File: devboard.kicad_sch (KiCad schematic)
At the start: 28 parts, among them J1 USB4110-GF-A, J2 USB_BOOT, P1 TC2030-CTX, U1 RP2040, U2 NCP1117-3.3_SOT223, U3 AT25SF128A-SHB-T, Y1 ECS-2033-120-BN

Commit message: finished??
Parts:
- added H1, H10, H11, H12, H3, H4, H5, H6, H7, H8, H9: MountingHole_Pad, MountingHole:MountingHole_2.2mm_M2_Pad, symbol Mechanical:MountingHole_Pad
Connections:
- net GND: now also H1.1, H10.1, H11.1, H12.1, H3.1, H4.1, H5.1, H6.1, H7.1, H8.1, H9.1

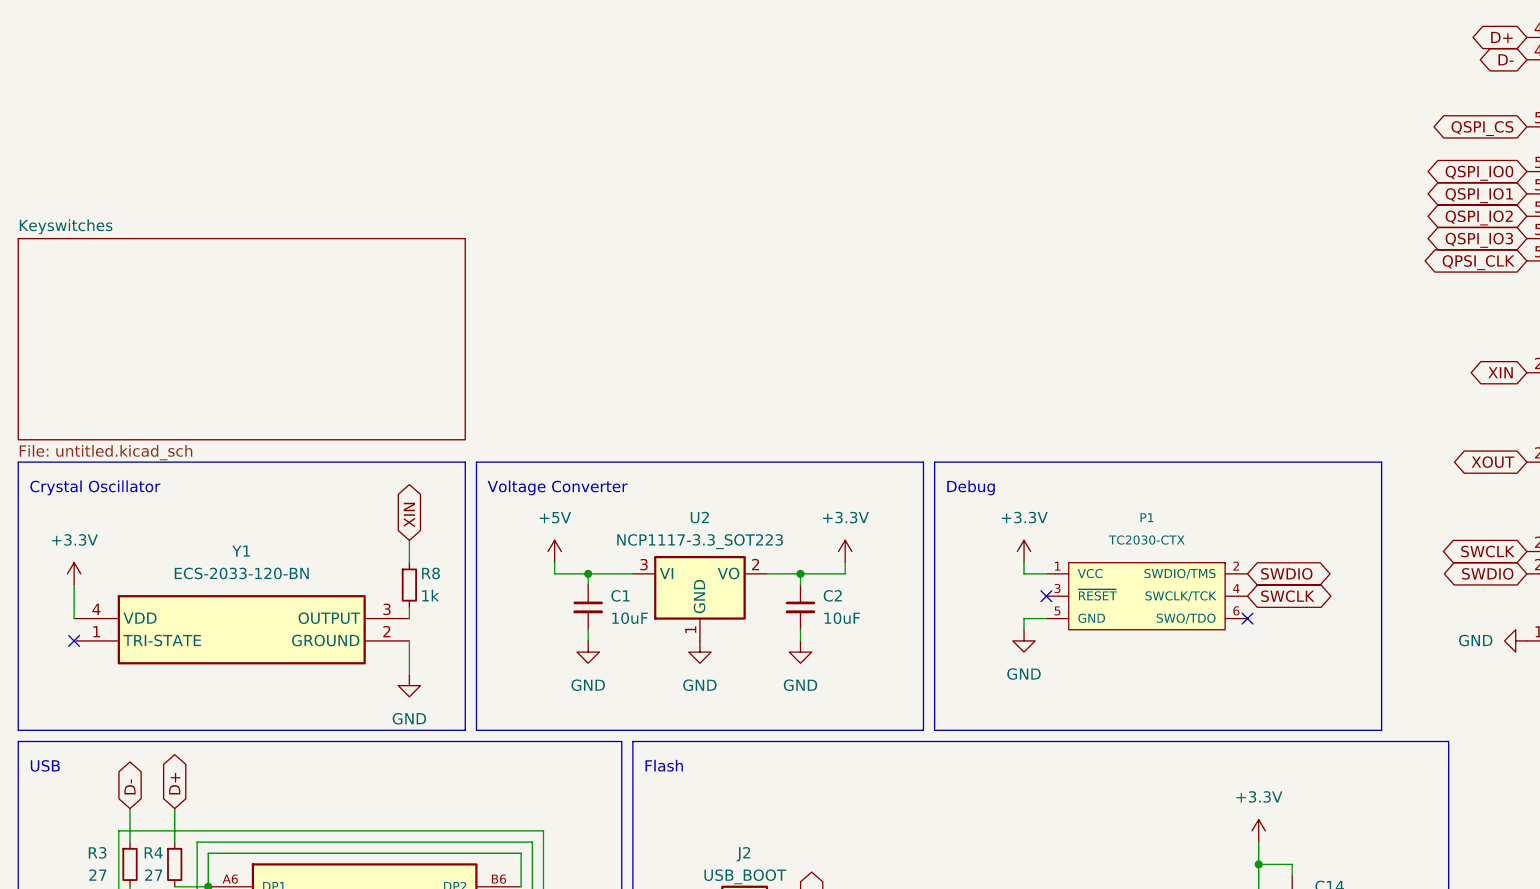
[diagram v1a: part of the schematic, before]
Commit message: Change LDO to DCDC Buck Converter
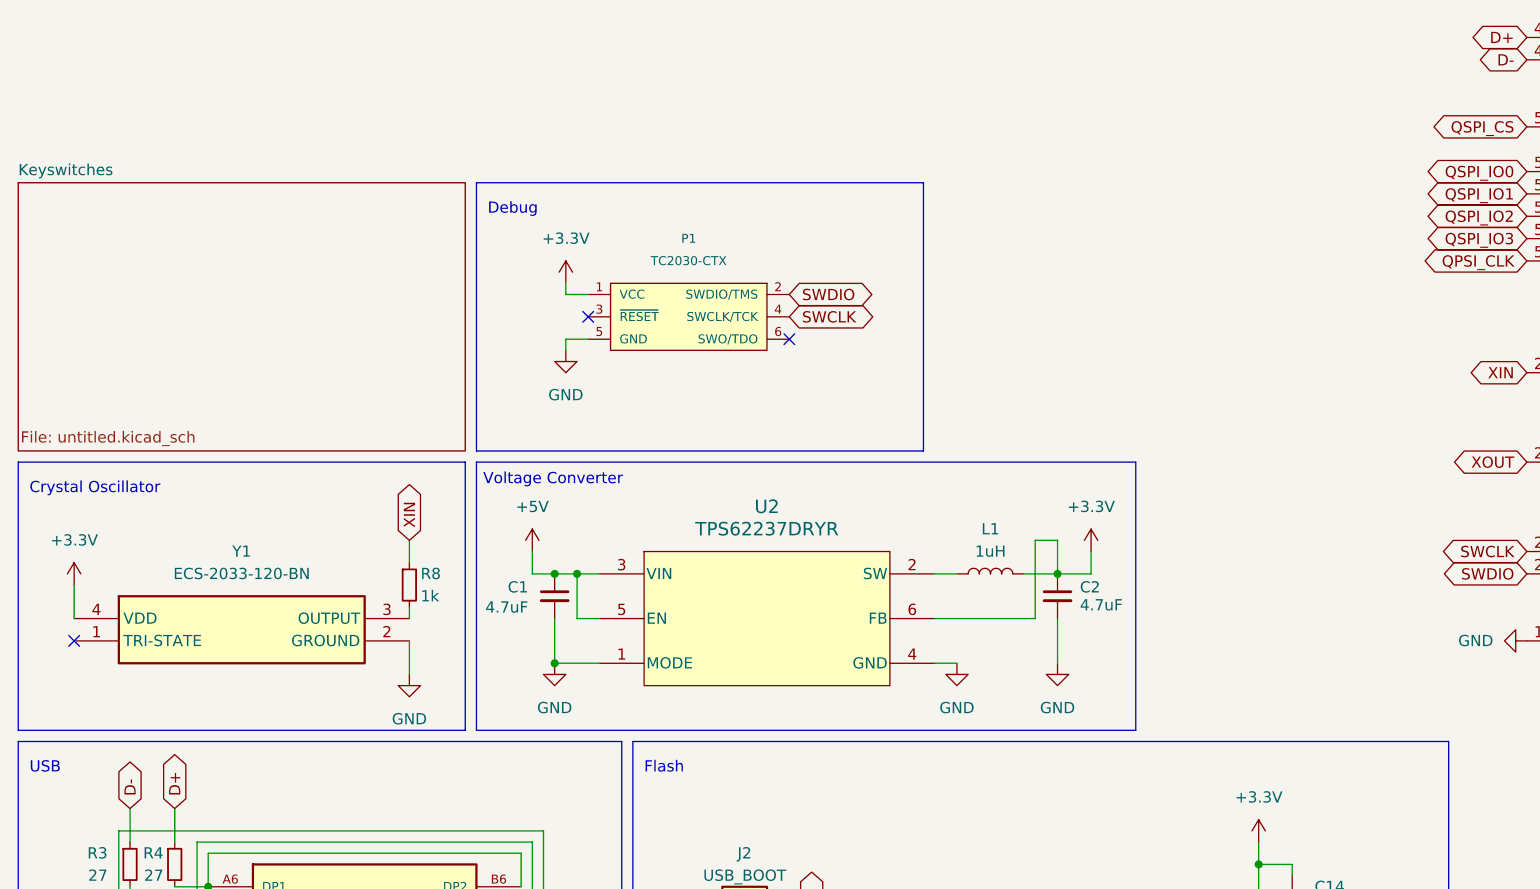
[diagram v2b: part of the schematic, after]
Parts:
- removed U2: NCP1117-3.3_SOT223, Package_TO_SOT_SMD:SOT-223-3_TabPin2, symbol Regulator_Linear:NCP1117-3.3_SOT223
- added L1: 1uH, Inductor_SMD:L_1008_2520Metric, symbol Device:L
- added U2: TPS62237DRYR, TPS62237:DRY0006A, symbol TPS62237:TPS62237DRYR
- C1, C2: value 10uF -> 4.7uF
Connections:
- net +3.3V: now also L1.2, U2.6 (FB)
- net +5V: now also U2.3 (VIN), U2.5 (EN)
- net GND: now also U2.1 (MODE), U2.4 (GND)
- new net: L1.1, U2.2 (SW)
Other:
- moved on the sheet: P1

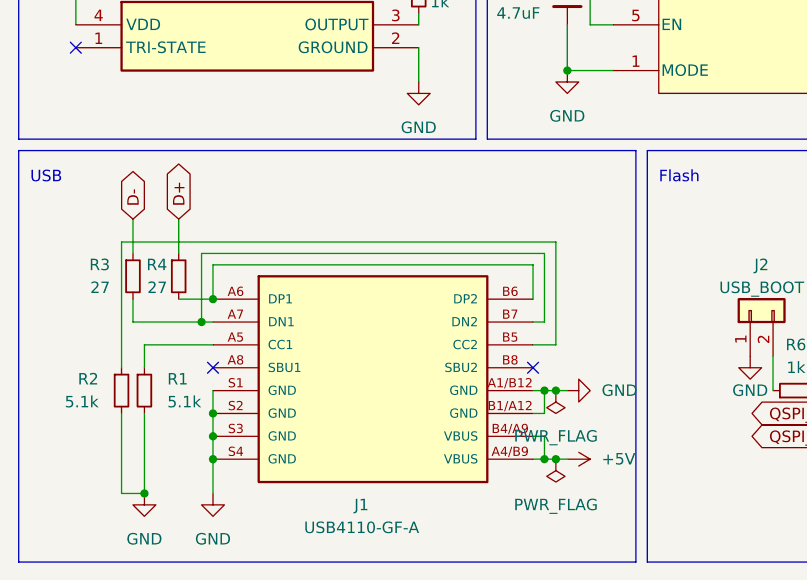
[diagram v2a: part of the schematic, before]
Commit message: Redo some routing and placement
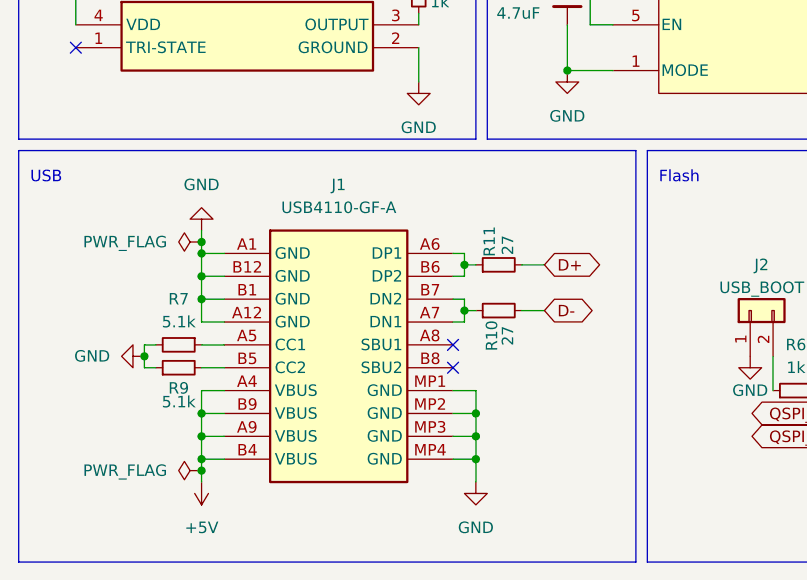
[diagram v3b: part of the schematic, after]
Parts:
- removed J1: USB4110-GF-A, 1A_Connectors:GCT_USB4110GFA, symbol 1A_Connectors:USB4110GFA
- removed R1, R2: 5.1k, Resistor_SMD:R_0402_1005Metric, symbol Device:R_Small
- removed R3, R4: 27, Resistor_SMD:R_0402_1005Metric, symbol Device:R_Small
- added J1: USB4110-GF-A, USB4110GFA, symbol SamacSys_Parts:USB4110-GF-A
- added R10, R11: 27, Resistor_SMD:R_0402_1005Metric, symbol Device:R_Small
- added R7, R9: 5.1k, Resistor_SMD:R_0402_1005Metric, symbol Device:R_Small
- P1: footprint 1A_Connectors:TC2030-IDC-NL -> SamacSys_Parts:TC2030MCPNL10
- U2: footprint TPS62237:DRY0006A -> SamacSys_Parts:TPS62237DRYR
- U3: footprint 1A_ICs:AT25SF128A-SHB-T -> SamacSys_Parts:SOIC127P798X216-8N
- Y1: footprint 1A_Oscillators:ECS-2033-120-BN -> SamacSys_Parts:ECS2033120BN
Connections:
- net +5V: now also J1.A4 (VBUS), J1.A9 (VBUS), J1.B4 (VBUS), J1.B9 (VBUS)
- net D+: now also R11.2
- net D-: now also R10.2
- net GND: now also J1.A1 (GND), J1.A12 (GND), J1.B1 (GND), J1.B12 (GND), J1.MP1 (GND), J1.MP2 (GND), J1.MP3 (GND), J1.MP4 (GND), R7.2, R9.1
- new net: J1.A5 (CC1), R7.1
- new net: J1.A6 (DP1), J1.B6 (DP2), R11.1
- new net: J1.A7 (DN1), J1.B7 (DN2), R10.1
- new net: J1.B5 (CC2), R9.2
